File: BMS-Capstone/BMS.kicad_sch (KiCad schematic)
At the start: 0 parts

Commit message: routing for TI chip
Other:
- sheet Monitoring ports: added GND; removed none
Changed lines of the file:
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@@
-	)
-	(junction
-		(at 53.34 124.46)
-		(diameter 0)
-		(color 0 0 0 0)
 	)
 	(junction
@@
 	(wire
 		(pts
-			(xy 143.51 52.07) (xy 143.51 139.7)
-		)
-		(stroke
-			(width 0)
-			(type default)
-		)
-	)
-	(wire
-		(pts
 			(xy 156.21 78.74) (xy 161.29 78.74)
 		)
@@
 	(wire
 		(pts
-			(xy 143.51 139.7) (xy 53.34 139.7)
-		)
-		(stroke
-			(width 0)
-			(type default)
-		)
-	)
-	(wire
-		(pts
 			(xy 106.68 119.38) (xy 152.4 119.38)
 		)
@@
 	(wire
 		(pts
+			(xy 161.29 52.07) (xy 151.13 52.07)
+		)
+		(stroke
+			(width 0)
+			(type default)
+		)
+	)
+	(wire
+		(pts
 			(xy 96.52 55.88) (xy 101.6 55.88)
 		)
@@
 	(wire
 		(pts
-			(xy 53.34 139.7) (xy 53.34 124.46)
-		)
-		(stroke
-			(width 0)
-			(type default)
-		)
-	)
-	(wire
-		(pts
 			(xy 66.04 121.92) (xy 55.88 121.92)
 		)
@@
 	(wire
 		(pts
+			(xy 151.13 106.68) (xy 106.68 106.68)
+		)
+		(stroke
+			(width 0)
+			(type default)
+		)
+	)
+	(wire
+		(pts
 			(xy 59.69 114.3) (xy 59.69 88.9)
 		)
@@
 	(wire
 		(pts
-			(xy 161.29 52.07) (xy 143.51 52.07)
-		)
-		(stroke
-			(width 0)
-			(type default)
-		)
-	)
-	(wire
-		(pts
 			(xy 58.42 116.84) (xy 58.42 90.17)
 		)
@@
 		(pts
 			(xy 106.68 101.6) (xy 149.86 101.6)
+		)
+		(stroke
+			(width 0)
+			(type default)
+		)
+	)
+	(wire
+		(pts
+			(xy 151.13 52.07) (xy 151.13 106.68)
 		)
 		(stroke
@@
 		)
 		(pin "5V" input
-			(at 106.68 105.41 0)
+			(at 106.68 104.14 0)
 			(effects
 				(font
@@
 			(effects
 				(font
+					(size 1.27 1.27)
+				)
+				(justify right)
+			)
+		)
+		(pin "GND" input
+			(at 106.68 106.68 0)
+			(effects
+				(font

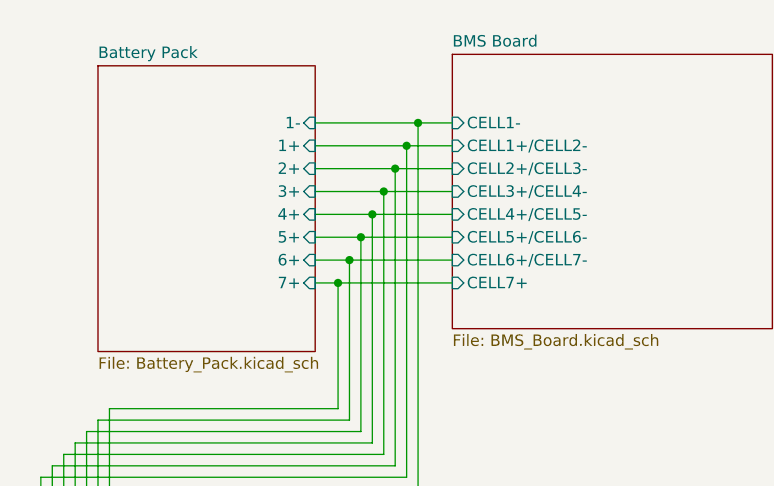
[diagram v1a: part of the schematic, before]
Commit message: Integrated in Monitoring board into final pcb
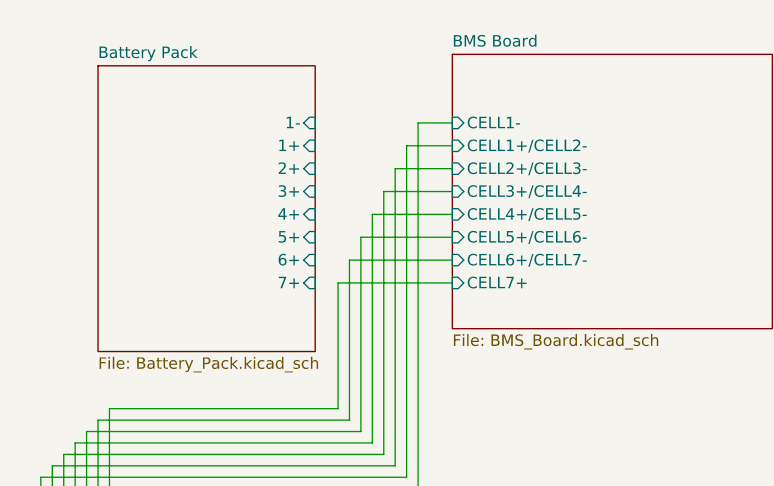
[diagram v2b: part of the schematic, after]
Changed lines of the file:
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@@
 	(generator_version "9.0")
 	(paper "A4")
-	(junction
-		(at 88.9 71.12)
-		(diameter 0)
-		(color 0 0 0 0)
-	)
-	(junction
-		(at 95.25 58.42)
-		(diameter 0)
-		(color 0 0 0 0)
-	)
-	(junction
-		(at 90.17 68.58)
-		(diameter 0)
-		(color 0 0 0 0)
-	)
-	(junction
-		(at 92.71 63.5)
-		(diameter 0)
-		(color 0 0 0 0)
-	)
-	(junction
-		(at 96.52 55.88)
-		(diameter 0)
-		(color 0 0 0 0)
-	)
-	(junction
-		(at 97.79 53.34)
-		(diameter 0)
-		(color 0 0 0 0)
-	)
-	(junction
-		(at 91.44 66.04)
-		(diameter 0)
-		(color 0 0 0 0)
-	)
-	(junction
-		(at 93.98 60.96)
-		(diameter 0)
-		(color 0 0 0 0)
-	)
 	(wire
 		(pts
@@
 	(wire
 		(pts
-			(xy 86.36 55.88) (xy 96.52 55.88)
-		)
-		(stroke
-			(width 0)
-			(type default)
-		)
-	)
-	(wire
-		(pts
 			(xy 59.69 88.9) (xy 92.71 88.9)
 		)
@@
 	(wire
 		(pts
-			(xy 86.36 60.96) (xy 93.98 60.96)
-		)
-		(stroke
-			(width 0)
-			(type default)
-		)
-	)
-	(wire
-		(pts
 			(xy 63.5 106.68) (xy 63.5 85.09)
 		)
@@
 	(wire
 		(pts
-			(xy 86.36 71.12) (xy 88.9 71.12)
-		)
-		(stroke
-			(width 0)
-			(type default)
-		)
-	)
-	(wire
-		(pts
 			(xy 154.94 124.46) (xy 106.68 124.46)
 		)
@@
 	(wire
 		(pts
-			(xy 86.36 58.42) (xy 95.25 58.42)
-		)
-		(stroke
-			(width 0)
-			(type default)
-		)
-	)
-	(wire
-		(pts
 			(xy 96.52 92.71) (xy 96.52 55.88)
 		)
@@
 	(wire
 		(pts
-			(xy 86.36 63.5) (xy 92.71 63.5)
-		)
-		(stroke
-			(width 0)
-			(type default)
-		)
-	)
-	(wire
-		(pts
-			(xy 86.36 53.34) (xy 97.79 53.34)
-		)
-		(stroke
-			(width 0)
-			(type default)
-		)
-	)
-	(wire
-		(pts
 			(xy 106.68 121.92) (xy 153.67 121.92)
 		)
@@
 	(wire
 		(pts
-			(xy 86.36 68.58) (xy 90.17 68.58)
-		)
-		(stroke
-			(width 0)
-			(type default)
-		)
-	)
-	(wire
-		(pts
 			(xy 91.44 87.63) (xy 91.44 66.04)
 		)
@@
 		)
 		(stroke
-			(width 0)
-			(type default)
-		)
-	)
-	(wire
-		(pts
-			(xy 86.36 66.04) (xy 91.44 66.04)
-		)
-		(stroke

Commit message: Final touches
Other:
- sheet BMS Board ports: added 1EN, 1MODE, 2EN, 2MODE, 3EN, 3MODE, 4EN, 4MODE, 5EN, 5MODE, 6EN, 6MODE, MCUGND, RELAY, TH1, TH2, TH3; removed none
- sheet Teensy 4.0 ports: added 1EN, 1MODE, 2EN, 2MODE, 3EN, 3MODE, 4EN, 4MODE, 5EN, 5MODE, 6EN, 6MODE, CS, INT, MISO, MOSI, RELAY, SCK, TH1, TH2, TH3; removed SCL0, SCL1, SDA0, SDA1

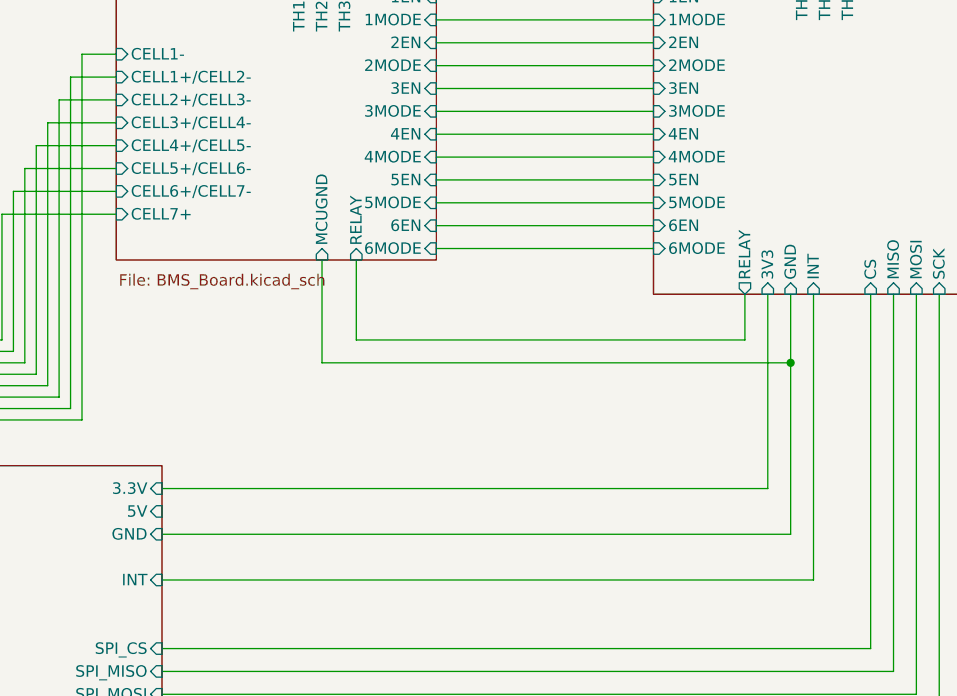
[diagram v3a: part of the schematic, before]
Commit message: Added Transistors for optocouple and relay drive
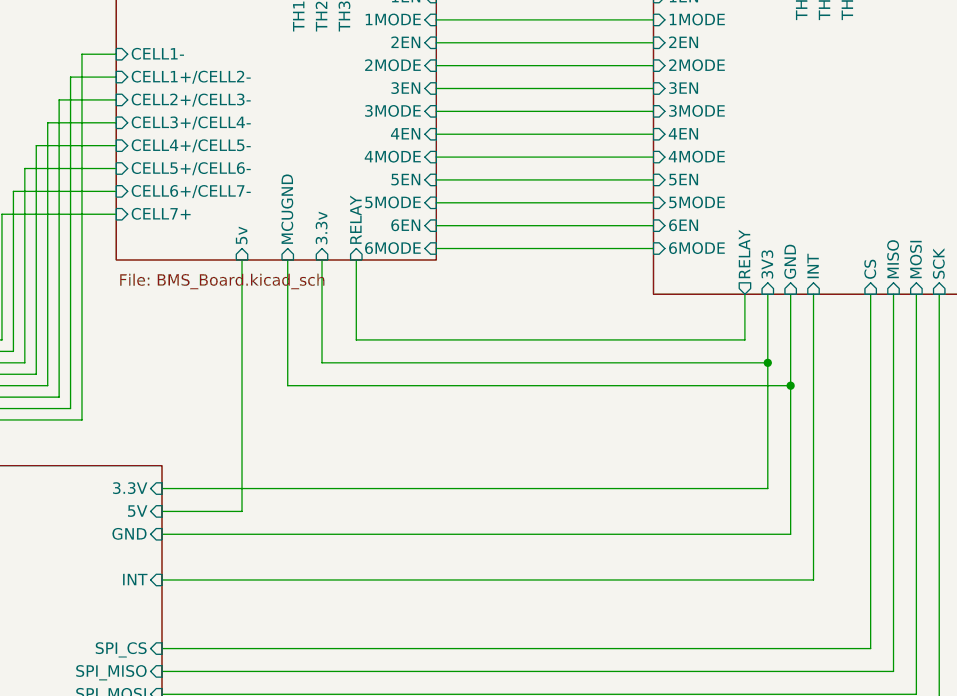
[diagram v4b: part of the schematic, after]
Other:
- sheet BMS Board ports: added 3.3v, 5v; removed none
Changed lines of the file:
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@@
 	(paper "A4")
 	(junction
-		(at 176.53 87.63)
+		(at 176.53 90.17)
 		(diameter 0)
 		(color 0 0 0 0)
 	)
+	(junction
+		(at 173.99 87.63)
+		(diameter 0)
+		(color 0 0 0 0)
+	)
 	(wire
 		(pts
@@
 	(wire
 		(pts
-			(xy 176.53 80.01) (xy 176.53 87.63)
+			(xy 176.53 80.01) (xy 176.53 90.17)
 		)
 		(stroke
@@
 	(wire
 		(pts
+			(xy 124.46 76.2) (xy 124.46 87.63)
+		)
+		(stroke
+			(width 0)
+			(type default)
+		)
+	)
+	(wire
+		(pts
 			(xy 137.16 62.23) (xy 161.29 62.23)
 		)
@@
 	(wire
 		(pts
+			(xy 115.57 104.14) (xy 115.57 76.2)
+		)
+		(stroke
+			(width 0)
+			(type default)
+		)
+	)
+	(wire
+		(pts
 			(xy 137.16 69.85) (xy 161.29 69.85)
 		)
@@
 	(wire
 		(pts
-			(xy 124.46 76.2) (xy 124.46 87.63)
+			(xy 120.65 76.2) (xy 120.65 90.17)
 		)
 		(stroke
@@
 	(wire
 		(pts
+			(xy 106.68 104.14) (xy 115.57 104.14)
+		)
+		(stroke
+			(width 0)
+			(type default)
+		)
+	)
+	(wire
+		(pts
 			(xy 90.17 68.58) (xy 101.6 68.58)
 		)
@@
 	(wire
 		(pts
-			(xy 176.53 87.63) (xy 176.53 106.68)
-		)
-		(stroke
-			(width 0)
-			(type default)
-		)
-	)
-	(wire
-		(pts
 			(xy 66.04 106.68) (xy 63.5 106.68)
 		)
@@
 	(wire
 		(pts
+			(xy 176.53 90.17) (xy 176.53 106.68)
+		)
+		(stroke
+			(width 0)
+			(type default)
+		)
+	)
+	(wire
+		(pts
 			(xy 176.53 106.68) (xy 106.68 106.68)
 		)
@@
 	(wire
 		(pts
+			(xy 173.99 87.63) (xy 173.99 80.01)
+		)
+		(stroke
+			(width 0)
+			(type default)
+		)
+	)
+	(wire
+		(pts
 			(xy 137.16 59.69) (xy 161.29 59.69)
 		)
@@
 	(wire
 		(pts
-			(xy 124.46 87.63) (xy 176.53 87.63)
+			(xy 120.65 90.17) (xy 176.53 90.17)
 		)
 		(stroke
@@
 	(wire
 		(pts
+			(xy 124.46 87.63) (xy 173.99 87.63)
+		)
+		(stroke
+			(width 0)
+			(type default)
+		)
+	)
+	(wire
+		(pts
 			(xy 106.68 101.6) (xy 173.99 101.6)
 		)
@@
 	(wire
 		(pts
-			(xy 173.99 101.6) (xy 173.99 80.01)
+			(xy 173.99 101.6) (xy 173.99 87.63)
 		)
 		(stroke
@@
 		)
 		(pin "MCUGND" input
-			(at 124.46 76.2 270)
+			(at 120.65 76.2 270)
 			(effects
 				(font
@@
 			(effects
 				(font
+					(size 1.27 1.27)
+				)
+				(justify left)
+			)
+		)
+		(pin "3.3v" input
+			(at 124.46 76.2 270)
+			(effects
+				(font
+					(size 1.27 1.27)
+				)
+				(justify left)
+			)
+		)
+		(pin "5v" input
+			(at 115.57 76.2 270)
+			(effects
+				(font
